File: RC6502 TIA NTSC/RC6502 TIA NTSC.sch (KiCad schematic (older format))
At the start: 45 parts, among them J1 Audio, J2 VDU_BASE, J3 Analog, J8 Composite, J9 RC6502_Backplane_Extra, U1 TIA_NTSC, U2 74HCT138, U3 VDU_Port, X1 3.579545 MHz

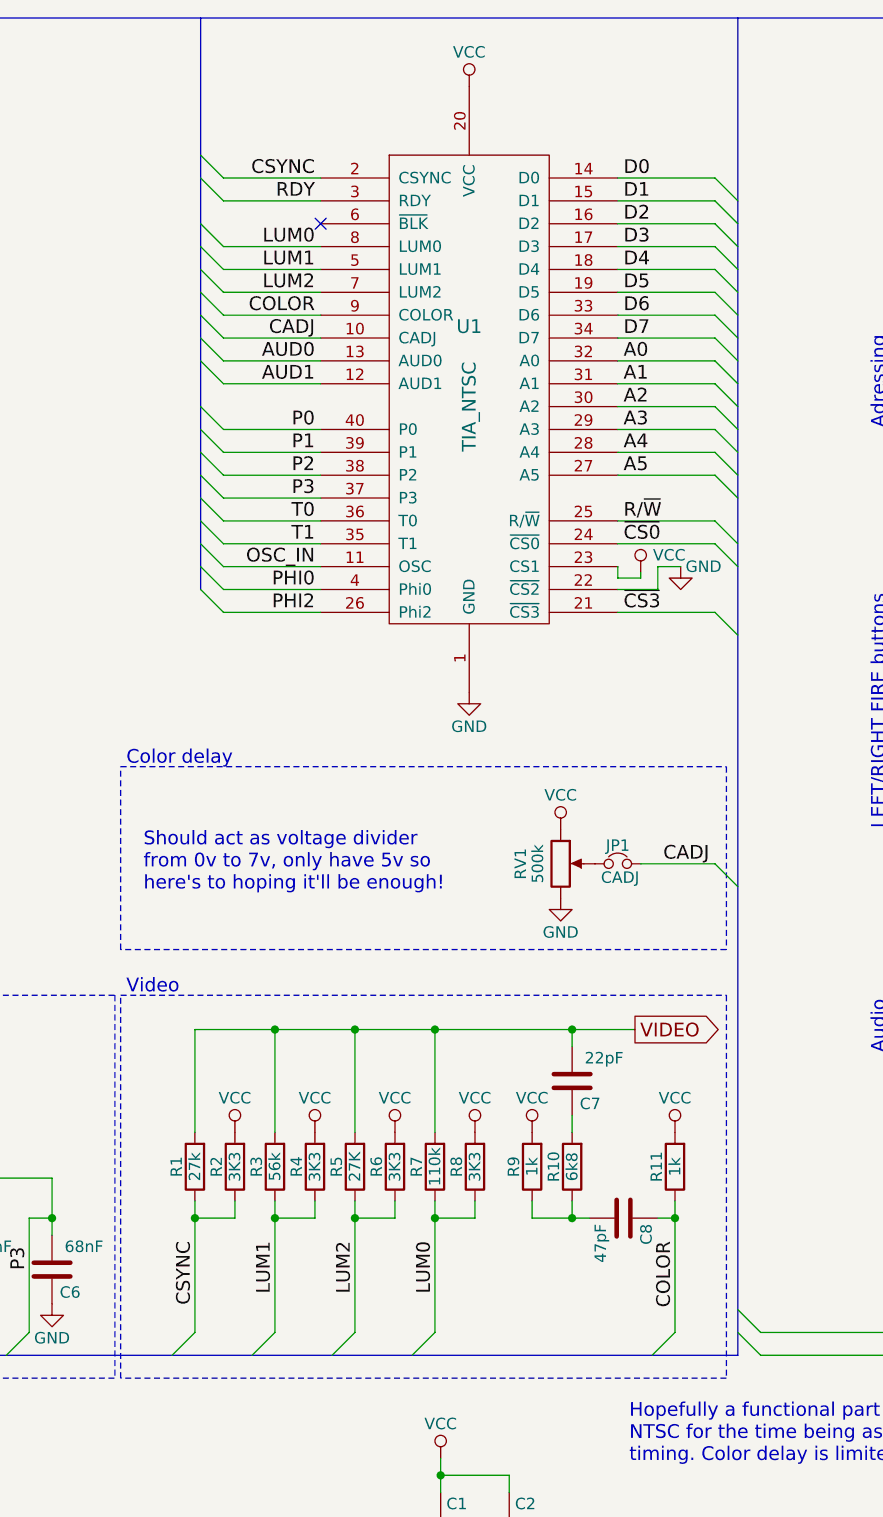
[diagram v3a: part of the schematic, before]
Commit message: Tweaked silkscreen
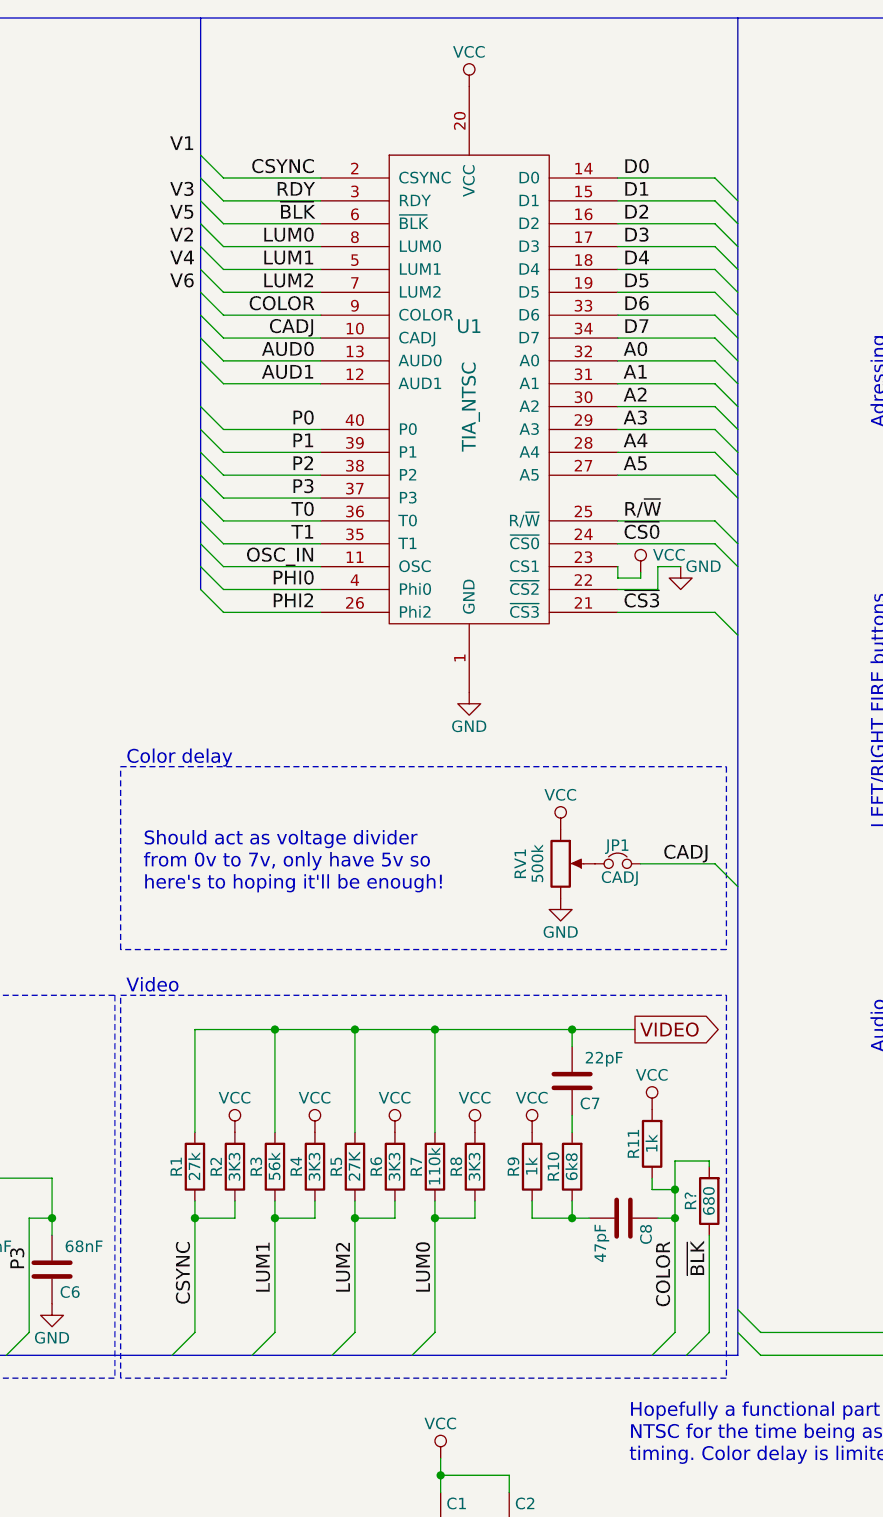
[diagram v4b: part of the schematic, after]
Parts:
- added R?: 680, Resistors_THT:R_Axial_DIN0207_L6.3mm_D2.5mm_P10.16mm_Horizontal, symbol R
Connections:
- net COLOR: now also R?.2
- net ~BLK: now reaches U1.6 (~BLK)
- net ~BLK: now also R?.1
- no-connect marks 14 -> 13
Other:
- moved on the sheet: R11
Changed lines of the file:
@@
 CSYNC
 Wire Wire Line
-	7200 5700 7200 6275
+	7200 5525 7200 6275
 Wire Wire Line
 	5100 5700 5100 6275
@@
 L R R11
 U 1 1 5C65E4DC
-P 7200 5550
-F 0 "R11" V 7280 5550 50  0000 C CNN
-F 1 "1k" V 7200 5550 50  0000 C CNN
-F 2 "Resistors_THT:R_Axial_DIN0207_L6.3mm_D2.5mm_P10.16mm_Horizontal" V 7130 5550 50  0001 C CNN
-F 3 "" H 7200 5550 50  0001 C CNN
-	1    7200 5550
+P 7100 5450
+F 0 "R11" V 7180 5450 50  0000 C CNN
+F 1 "1k" V 7100 5450 50  0000 C CNN
+F 2 "Resistors_THT:R_Axial_DIN0207_L6.3mm_D2.5mm_P10.16mm_Horizontal" V 7030 5450 50  0001 C CNN
+F 3 "" H 7100 5450 50  0001 C CNN
+	1    7100 5450
 	-1   0    0    1
 $EndComp
@@
 L VCC #PWR027
 U 1 1 5C65F6C2
-P 7200 5400
-F 0 "#PWR027" H 7200 5250 50  0001 C CNN
-F 1 "VCC" H 7200 5550 50  0000 C CNN
-F 2 "" H 7200 5400 50  0001 C CNN
-F 3 "" H 7200 5400 50  0001 C CNN
-	1    7200 5400
+P 7100 5300
+F 0 "#PWR027" H 7100 5150 50  0001 C CNN
+F 1 "VCC" H 7100 5450 50  0000 C CNN
+F 2 "" H 7100 5300 50  0001 C CNN
+F 3 "" H 7100 5300 50  0001 C CNN
+	1    7100 5300
 	1    0    0    -1
 $EndComp
@@
 VIDEO
 Connection ~ 6750 4950
-NoConn ~ 5650 1425
 Wire Wire Line
 	5650 2625 5225 2625
@@
 NoConn ~ 10400 3150
 NoConn ~ 10400 3350
+Text Label 5100 1125 2    60   ~ 0
+V1
+Text Label 5100 1525 2    60   ~ 0
+V2
+Text Label 5100 1325 2    60   ~ 0
+V3
+Text Label 5100 1625 2    60   ~ 0
+V4
+Text Label 5100 1425 2    60   ~ 0
+V5
+Text Label 5100 1725 2    60   ~ 0
+V6
+Text Label 5625 1425 2    60   ~ 0
+~BLK
+Wire Wire Line
+	5650 1425 5225 1425
+Entry Wire Line
+	5225 1425 5125 1325
+Text Label 7350 5875 3    60   ~ 0
+~BLK
+Entry Wire Line
+	7350 6275 7250 6375
+$Comp
+L R R?
+U 1 1 5C8311A5
+P 7350 5700
+F 0 "R?" V 7430 5700 50  0000 C CNN
+F 1 "680" V 7350 5700 50  0000 C CNN
+F 2 "Resistors_THT:R_Axial_DIN0207_L6.3mm_D2.5mm_P10.16mm_Horizontal" V 7280 5700 50  0001 C CNN
+F 3 "" H 7350 5700 50  0001 C CNN
+	1    7350 5700
+	-1   0    0    1
+$EndComp
+Wire Wire Line
+	7350 5550 7350 5525
+Wire Wire Line
+	7350 5525 7200 5525
+Wire Wire Line
+	7100 5600 7100 5650
+Wire Wire Line
+	7100 5650 7200 5650
+Connection ~ 7200 5650
+Wire Wire Line
+	7350 5850 7350 6275
 $EndSCHEMATC
